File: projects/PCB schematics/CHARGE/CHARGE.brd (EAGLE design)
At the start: 99.1 x 99.1 mm, 24 parts, among them Q1 IRLZ44Z, Q2 IRLZ44Z, Q3 IRLZ44Z, X1 5566-2, X3 5566-2, X4 5566-8

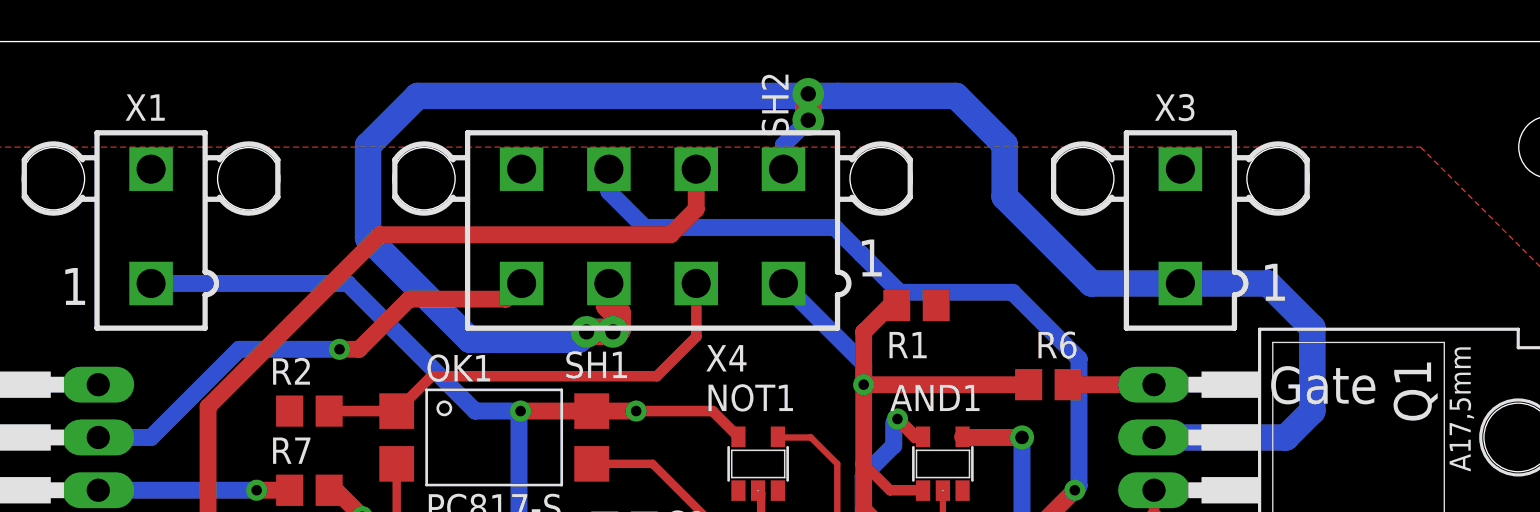
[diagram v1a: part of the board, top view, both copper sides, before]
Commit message: PROJ - Silkscreen modifications - 50%.
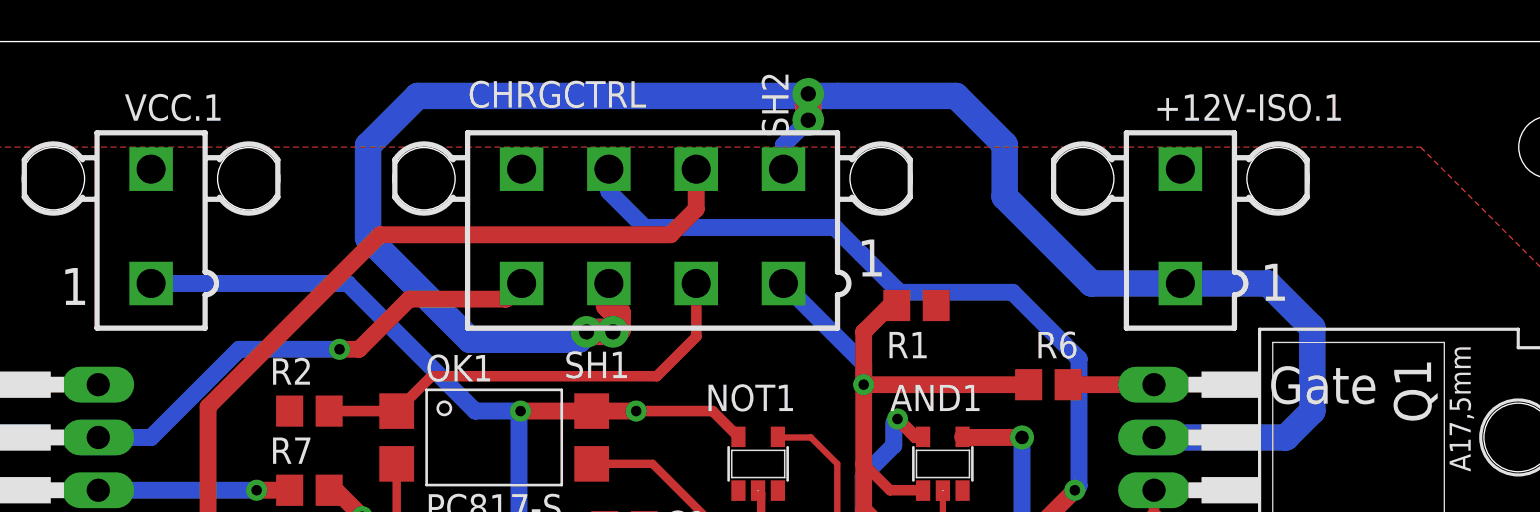
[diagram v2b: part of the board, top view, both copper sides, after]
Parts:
- renumbered X1 to VCC.1, X3 to +12V-ISO.1, X4 to CHRGCTRL
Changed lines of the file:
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@@
 <attribute name="VALUE" x="15.24" y="64.643" size="1.778" layer="27" ratio="10" rot="R90"/>
 </element>
-<element name="X1" library="con-molex" library_urn="urn:adsk.eagle:library:165" package="5566-2" package3d_urn="urn:adsk.eagle:package:8078583/1" value="5566-2" x="26.67" y="90.17" smashed="yes">
+<element name="VCC.1" library="con-molex" library_urn="urn:adsk.eagle:library:165" package="5566-2" package3d_urn="urn:adsk.eagle:package:8078583/1" value="5566-2" x="26.67" y="90.17" smashed="yes">
 <attribute name="MF" value="MOLEX" x="63.5" y="58.42" size="1.778" layer="27" display="off"/>
 <attribute name="MPN" value="" x="63.5" y="58.42" size="1.778" layer="27" display="off"/>
@@
 <attribute name="VALUE" x="24.13" y="83.82" size="1.27" layer="27"/>
 </element>
-<element name="X3" library="con-molex" library_urn="urn:adsk.eagle:library:165" package="5566-2" package3d_urn="urn:adsk.eagle:package:8078583/1" value="5566-2" x="76.2" y="90.17" smashed="yes">
+<element name="+12V-ISO.1" library="con-molex" library_urn="urn:adsk.eagle:library:165" package="5566-2" package3d_urn="urn:adsk.eagle:package:8078583/1" value="5566-2" x="76.2" y="90.17" smashed="yes">
 <attribute name="MF" value="MOLEX" x="76.2" y="90.17" size="1.778" layer="27" display="off"/>
 <attribute name="MPN" value="" x="76.2" y="90.17" size="1.778" layer="27" display="off"/>
@@
 <attribute name="VALUE" x="69.215" y="80.01" size="1.27" layer="27"/>
 </element>
-<element name="X4" library="con-molex" library_urn="urn:adsk.eagle:library:165" package="5566-8" package3d_urn="urn:adsk.eagle:package:8078580/1" value="5566-8" x="50.8" y="90.17" smashed="yes">
+<element name="CHRGCTRL" library="con-molex" library_urn="urn:adsk.eagle:library:165" package="5566-8" package3d_urn="urn:adsk.eagle:package:8078580/1" value="5566-8" x="50.8" y="90.17" smashed="yes">
 <attribute name="MF" value="MOLEX" x="50.8" y="90.17" size="1.778" layer="27" display="off"/>
 <attribute name="MPN" value="" x="50.8" y="90.17" size="1.778" layer="27" display="off"/>
-<attribute name="NAME" x="53.34" y="83.185" size="1.27" layer="25"/>
+<attribute name="NAME" x="41.91" y="95.885" size="1.27" layer="25"/>
 <attribute name="OC_FARNELL" value="unknown" x="50.8" y="90.17" size="1.778" layer="27" display="off"/>
 <attribute name="OC_NEWARK" value="unknown" x="50.8" y="90.17" size="1.778" layer="27" display="off"/>
@@
 <signal name="GND">
 <contactref element="Q3" pad="S"/>
-<contactref element="X1" pad="2"/>
-<contactref element="X3" pad="2"/>
+<contactref element="VCC.1" pad="2"/>
+<contactref element="+12V-ISO.1" pad="2"/>
 <contactref element="R5" pad="1"/>
 <contactref element="AND1" pad="3"/>
@@
 <wire x1="62.23" y1="86.36" x2="62.55" y2="86.36" width="0.508" layer="1"/>
 <via x="60.96" y="82.55" extent="1-16" drill="0.508"/>
-<contactref element="X4" pad="1"/>
+<contactref element="CHRGCTRL" pad="1"/>
 <contactref element="R6" pad="1"/>
 <contactref element="R7" pad="1"/>
@@
 <signal name="PRECHARGE_KEY12V">
 <contactref element="F1" pad="2"/>
-<contactref element="X4" pad="7"/>
+<contactref element="CHRGCTRL" pad="7"/>
 <wire x1="68.195" y1="71.12" x2="68.195" y2="74.545" width="0.8128" layer="1"/>
 <wire x1="68.195" y1="74.545" x2="71.12" y2="77.47" width="0.8128" layer="1"/>
@@
 </signal>
 <signal name="+12V-ISO">
-<contactref element="X3" pad="1"/>
+<contactref element="+12V-ISO.1" pad="1"/>
 <contactref element="Q1" pad="D"/>
 <wire x1="82.55" y1="85.2864" x2="80.4164" y2="87.42" width="1.27" layer="16"/>
@@
 <wire x1="40.1639" y1="82.9564" x2="51.0032" y2="82.9564" width="0.508" layer="1"/>
 <wire x1="51.0032" y1="82.9564" x2="52.9082" y2="84.8614" width="0.508" layer="1"/>
-<contactref element="X4" pad="2"/>
+<contactref element="CHRGCTRL" pad="2"/>
 <wire x1="52.9082" y1="84.8614" x2="52.9082" y2="87.4118" width="0.508" layer="1"/>
 <wire x1="52.9082" y1="87.4118" x2="52.9" y2="87.42" width="0.508" layer="1"/>
@@
 <signal name="VCC">
 <contactref element="AND1" pad="5"/>
-<contactref element="X1" pad="1"/>
+<contactref element="VCC.1" pad="1"/>
 <contactref element="NOT1" pad="5"/>
 <contactref element="OK1" pad="4"/>
@@
 <wire x1="29.4132" y1="81.4832" x2="37.6936" y2="89.7636" width="0.8128" layer="1"/>
 <wire x1="37.6936" y1="89.7636" x2="51.6636" y2="89.7636" width="0.8128" layer="1"/>
-<contactref element="X4" pad="6"/>
+<contactref element="CHRGCTRL" pad="6"/>
 <wire x1="52.9" y1="92.92" x2="52.9" y2="91" width="0.8128" layer="1"/>
 <wire x1="52.9" y1="91" x2="51.6636" y2="89.7636" width="0.8128" layer="1"/>
@@
 </signal>
 <signal name="AIR-_COIL+">
-<contactref element="X4" pad="3"/>
+<contactref element="CHRGCTRL" pad="3"/>
 <contactref element="SH1" pad="2"/>
 <wire x1="48.7" y1="87.42" x2="48.7" y2="86.40110625" width="1.27" layer="1"/>
@@
 </signal>
 <signal name="AIR-_COIL-">
-<contactref element="X4" pad="4"/>
+<contactref element="CHRGCTRL" pad="4"/>
 <contactref element="Q2" pad="D"/>
 <wire x1="24.13" y1="80.01" x2="26.67" y2="80.01" width="0.8128" layer="16"/>
@@
 </signal>
 <signal name="DISCHARGE_COIL+">
-<contactref element="X4" pad="5"/>
+<contactref element="CHRGCTRL" pad="5"/>
 <contactref element="SH2" pad="2"/>
 <wire x1="58.293" y1="95.2754" x2="57.1" y2="94.0824" width="0.8128" layer="16"/>

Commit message: PROJ - Final pre-purchase revisions (4 boards still in progress.)
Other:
- board text added: "Inputs (CHRGCTRL):"
- board text removed: "Inputs (X2):"
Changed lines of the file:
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@@
 <wire x1="66.2686" y1="38.9636" x2="63.373" y2="38.9636" width="0.254" layer="25"/>
 <text x="55.8546" y="32.3596" size="2.54" layer="25" font="vector">Iowa Formula</text>
-<text x="56.261" y="29.2354" size="1.4224" layer="25" font="vector">Inputs (X2):</text>
-<text x="56.1594" y="18.9992" size="0.9144" layer="25">1. AIR_CONTROL
+<text x="51.181" y="29.2354" size="1.4224" layer="25" font="vector">Inputs (CHRGCTRL):</text>
+<text x="51.0794" y="18.9992" size="0.9144" layer="25">1. AIR_CONTROL
 2. AIR+_COIL+
 3. AIR-_COIL+
@@
 6. DISCHARGE_COIL-
 7. PRECHARGE_KEY12V</text>
-<wire x1="56.1086" y1="28.8544" x2="67.9958" y2="28.8544" width="0.1524" layer="25"/>
+<wire x1="51.0286" y1="28.8544" x2="67.9958" y2="28.8544" width="0.1524" layer="25"/>
 <text x="24.9174" y="12.8778" size="1.778" layer="25" font="vector">Pre-charge Control (CHARGE) Board
 Rev A: 04/08/19</text>

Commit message: PROJ - Gerber files major milestone - 05/05/19.
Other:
- board text added: "Pre-charge Control (CHARGE) Board Rev A: 05/05/19"
- board text removed: "Pre-charge Control (CHARGE) Board Rev A: 04/08/19"
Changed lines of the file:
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@@
 <wire x1="51.0286" y1="28.8544" x2="67.9958" y2="28.8544" width="0.1524" layer="25"/>
 <text x="24.9174" y="12.8778" size="1.778" layer="25" font="vector">Pre-charge Control (CHARGE) Board
-Rev A: 04/08/19</text>
+Rev A: 05/05/19</text>
 <text x="46.355" y="13.716" size="0.9144" layer="25">Author: github.com/michaelpass</text>
 <text x="71.501" y="29.2354" size="1.4224" layer="25" font="vector">Power:</text>
@@
 <contactref element="CHRGCTRL" pad="3"/>
 <contactref element="SH1" pad="2"/>
-<wire x1="48.7" y1="87.42" x2="48.7" y2="86.40110625" width="1.27" layer="1"/>
-<wire x1="48.7" y1="86.40110625" x2="49.1236" y2="85.97750625" width="1.27" layer="1"/>
-<wire x1="49.1236" y1="85.97750625" x2="49.1236" y2="85.21849375" width="1.27" layer="1"/>
-<wire x1="49.1236" y1="85.21849375" x2="48.9966" y2="85.09149375" width="1.27" layer="1"/>
-<wire x1="48.9966" y1="85.09149375" x2="48.9966" y2="85.09" width="0.8128" layer="1"/>
-<wire x1="48.9966" y1="85.09149375" x2="48.895" y2="85.09" width="0" layer="19" extent="1-1"/>
+<wire x1="48.7" y1="85.285" x2="48.895" y2="85.09" width="1.27" layer="1"/>
+<wire x1="48.7" y1="87.42" x2="48.7" y2="85.285" width="1.27" layer="1"/>
 </signal>
 <signal name="AIR-_COIL-">
